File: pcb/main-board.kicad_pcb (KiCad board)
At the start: 2 copper layers, 21 x 45.5 mm, 6 parts

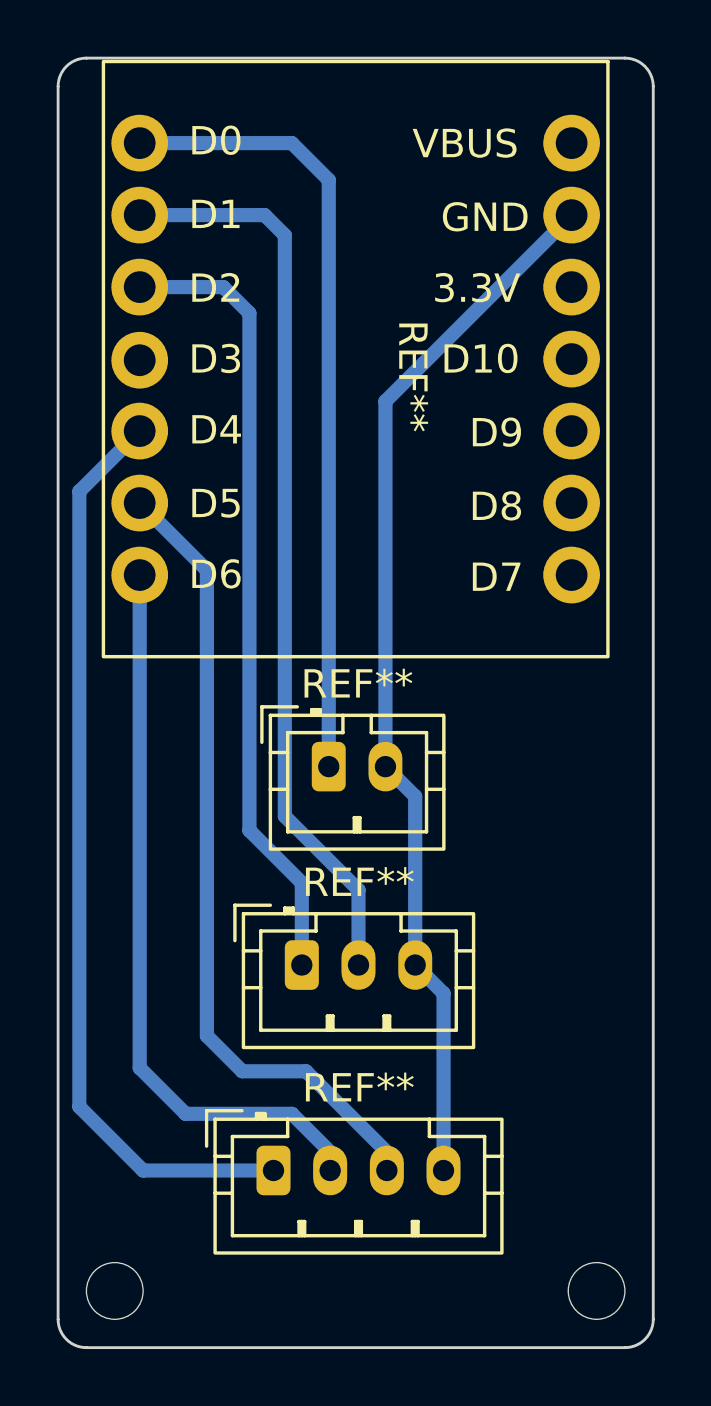
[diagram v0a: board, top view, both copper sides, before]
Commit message: add nc and chenge uf2 for studio
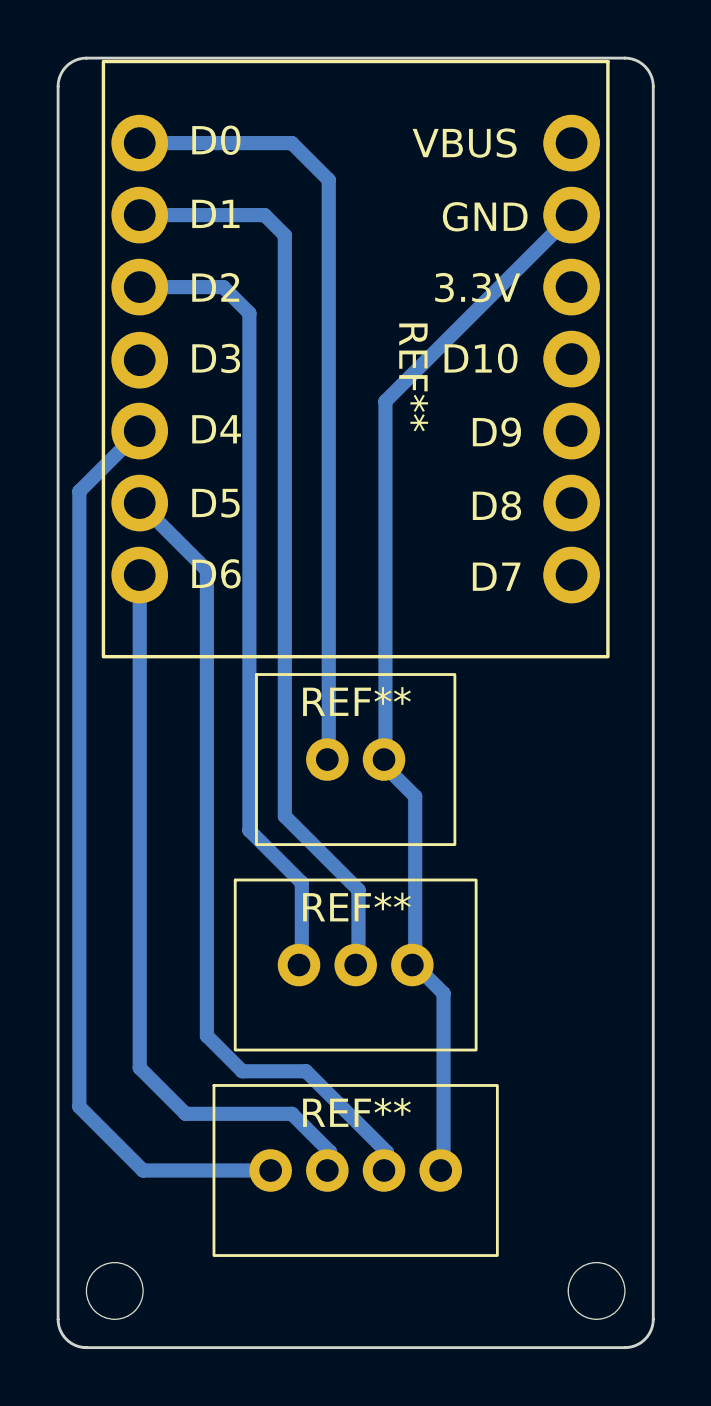
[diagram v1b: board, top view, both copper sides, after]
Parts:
- removed the REF** at (97.1, 103.8)
- removed the REF** at (98.1, 96.5)
- removed the REF** at (99.0, 89.5)
- added REF**: JST-PH-2-V, Suzuki:JstPh4Vertical, F.Cu at (100.0, 103.8)
- added REF**: JST-PH-2-V, Suzuki:JstPh3Vertical, F.Cu at (100.0, 96.5)
- added REF**: JST-PH-2-V, Suzuki:JstPh2Vertical, F.Cu at (100.0, 89.2)
